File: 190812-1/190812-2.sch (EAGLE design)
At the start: 18 parts, among them U1 MCP6071T-E/OT, U2 ESPRUINO_PICO_SMDONLY

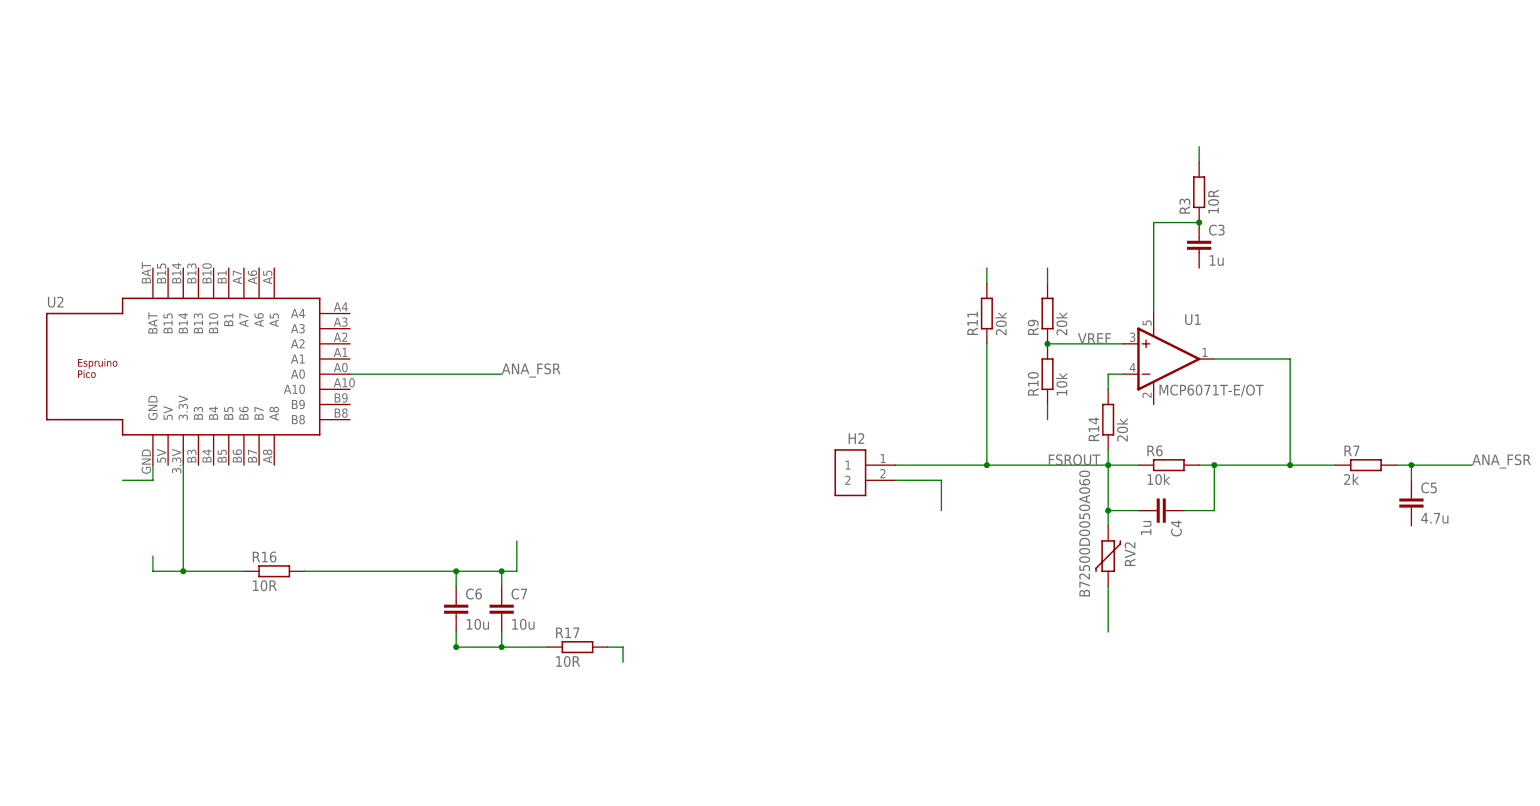
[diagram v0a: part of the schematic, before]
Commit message: Fixed schematic corruption.  Reran CAM.
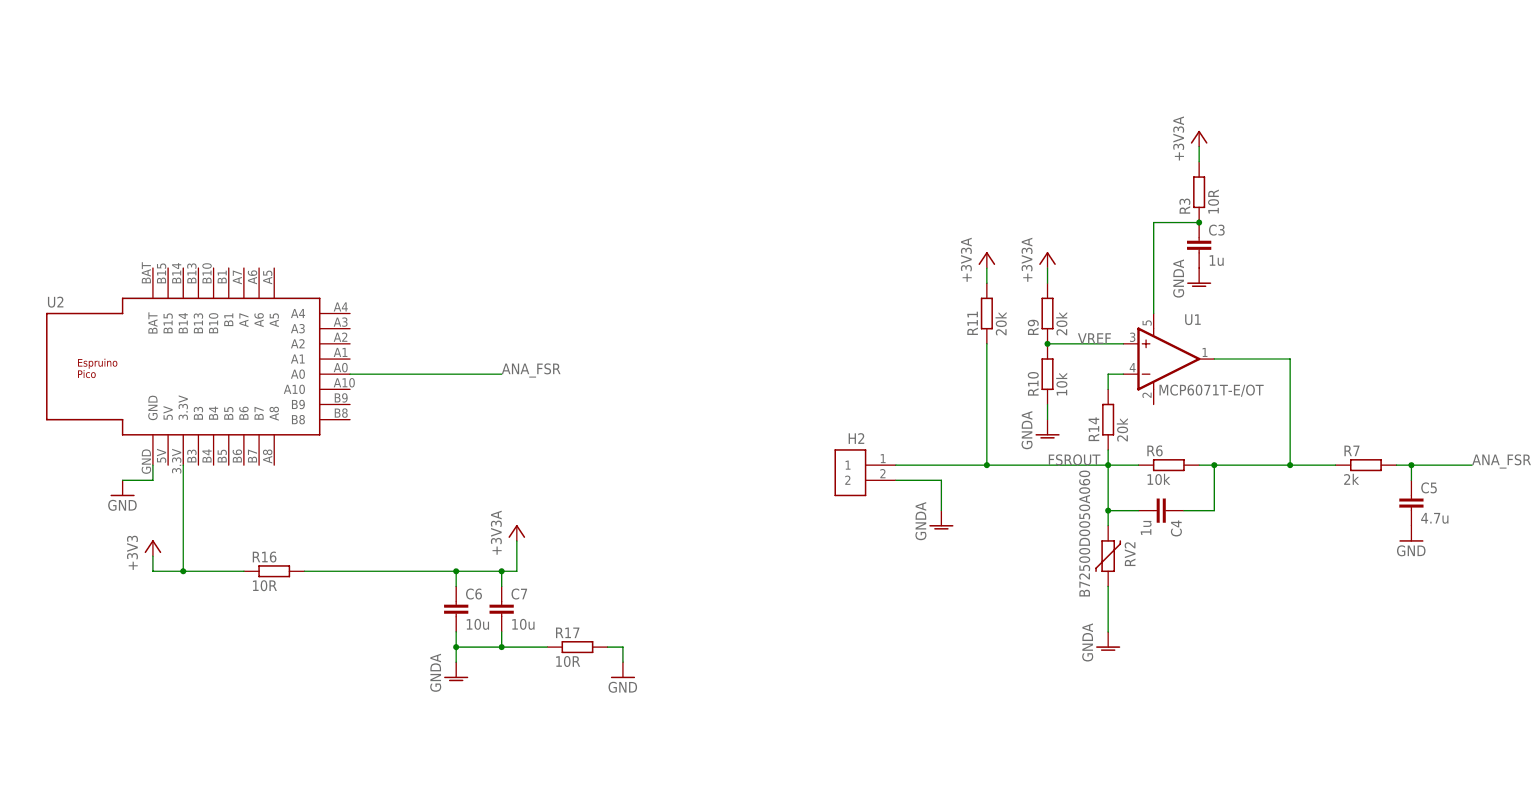
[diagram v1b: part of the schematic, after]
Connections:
- net +3V1 renamed +3V3
- net +3V3A1 renamed +3V3A
- net GND1 renamed GND
- new net GNDA: C3.2, C6.2, C7.2, H2.2, R10.1, R17.1, RV2.1
- net GNDA1: no longer C3.2, C6.2, C7.2, H2.2, R10.1, R17.1, RV2.1

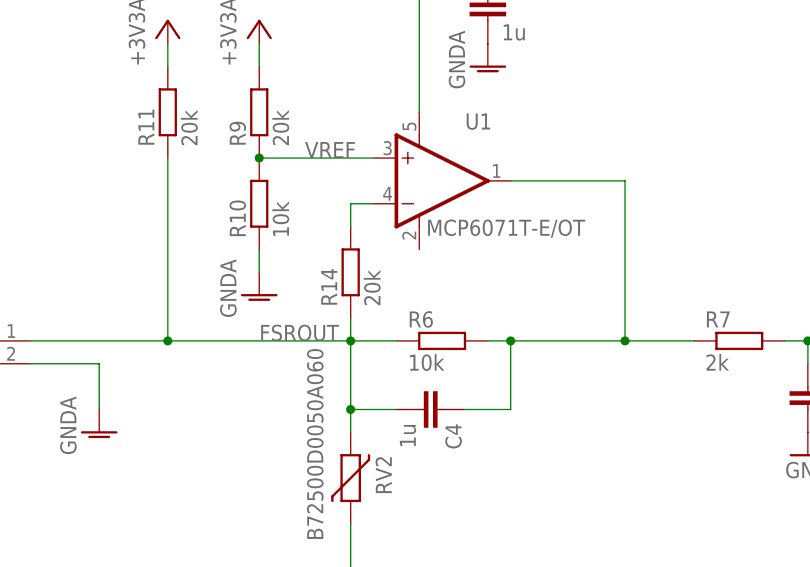
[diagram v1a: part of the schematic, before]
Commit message: added espruino code.  WARNING eagle was corrupted double check.
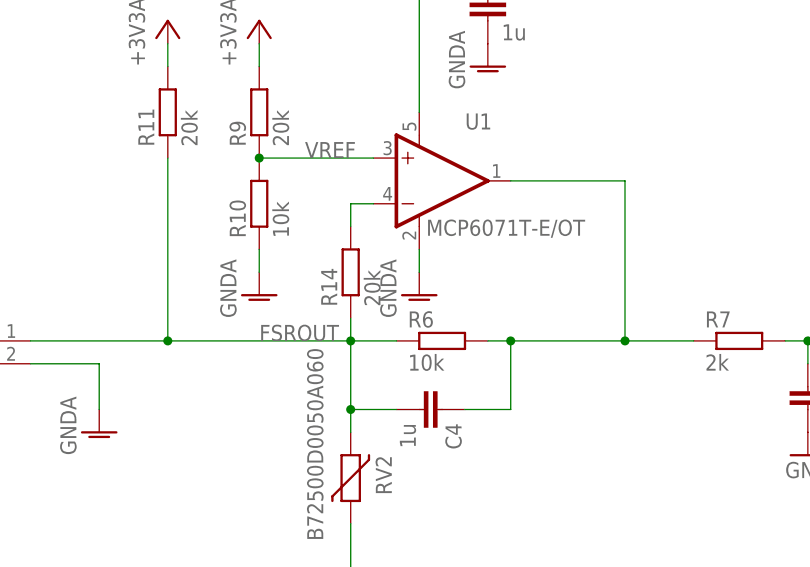
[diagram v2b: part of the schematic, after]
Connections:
- removed net GNDA1: U1.V-
- net GNDA: now also U1.V-
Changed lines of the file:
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@@
 <part name="+3V3A4" library="pwr-symbols-rmg" library_urn="urn:adsk.eagle:library:1326622" deviceset="+3V3A" device=""/>
 <part name="GND3" library="supply1" library_urn="urn:adsk.eagle:library:371" deviceset="GND" device=""/>
+<part name="GNDA6" library="pwr-symbols-rmg" library_urn="urn:adsk.eagle:library:1326622" deviceset="GNDA" device=""/>
 </parts>
 <sheets>
@@
 <instance part="GND3" gate="1" x="302.26" y="114.3" smashed="yes">
 <attribute name="VALUE" x="299.72" y="111.76" size="1.778" layer="96"/>
+</instance>
+<instance part="GNDA6" gate="1" x="259.08" y="132.08" smashed="yes">
+<attribute name="VALUE" x="256.54" y="129.54" size="1.778" layer="96" rot="R90"/>
 </instance>
 </instances>
@@
 </segment>
 </net>
-<net name="GNDA1" class="0">
-<segment>
-<pinref part="U1" gate="G$1" pin="V-"/>
-</segment>
-</net>
 <net name="VREF" class="0">
 <segment>
@@
 <pinref part="GNDA5" gate="1" pin="GNDA"/>
 </segment>
-</net>
+<segment>
+<pinref part="U1" gate="G$1" pin="V-"/>
+<pinref part="GNDA6" gate="1" pin="GNDA"/>
+<wire x1="259.08" y1="134.62" x2="259.08" y2="137.16" width="0.1524" layer="91"/>
+</segment>
+</net>
